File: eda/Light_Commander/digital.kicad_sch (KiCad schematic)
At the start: 40 parts, among them J14 USB_C_Receptacle_USB2.0_16P, J18 Conn_01x03, SW2 SW_Push, U1 STM32F446RETx, U10 6N137, U11 NXU0101GW, U6 USBLC6-2SC6, U8 NXU0101GW, Y1 8 MHz

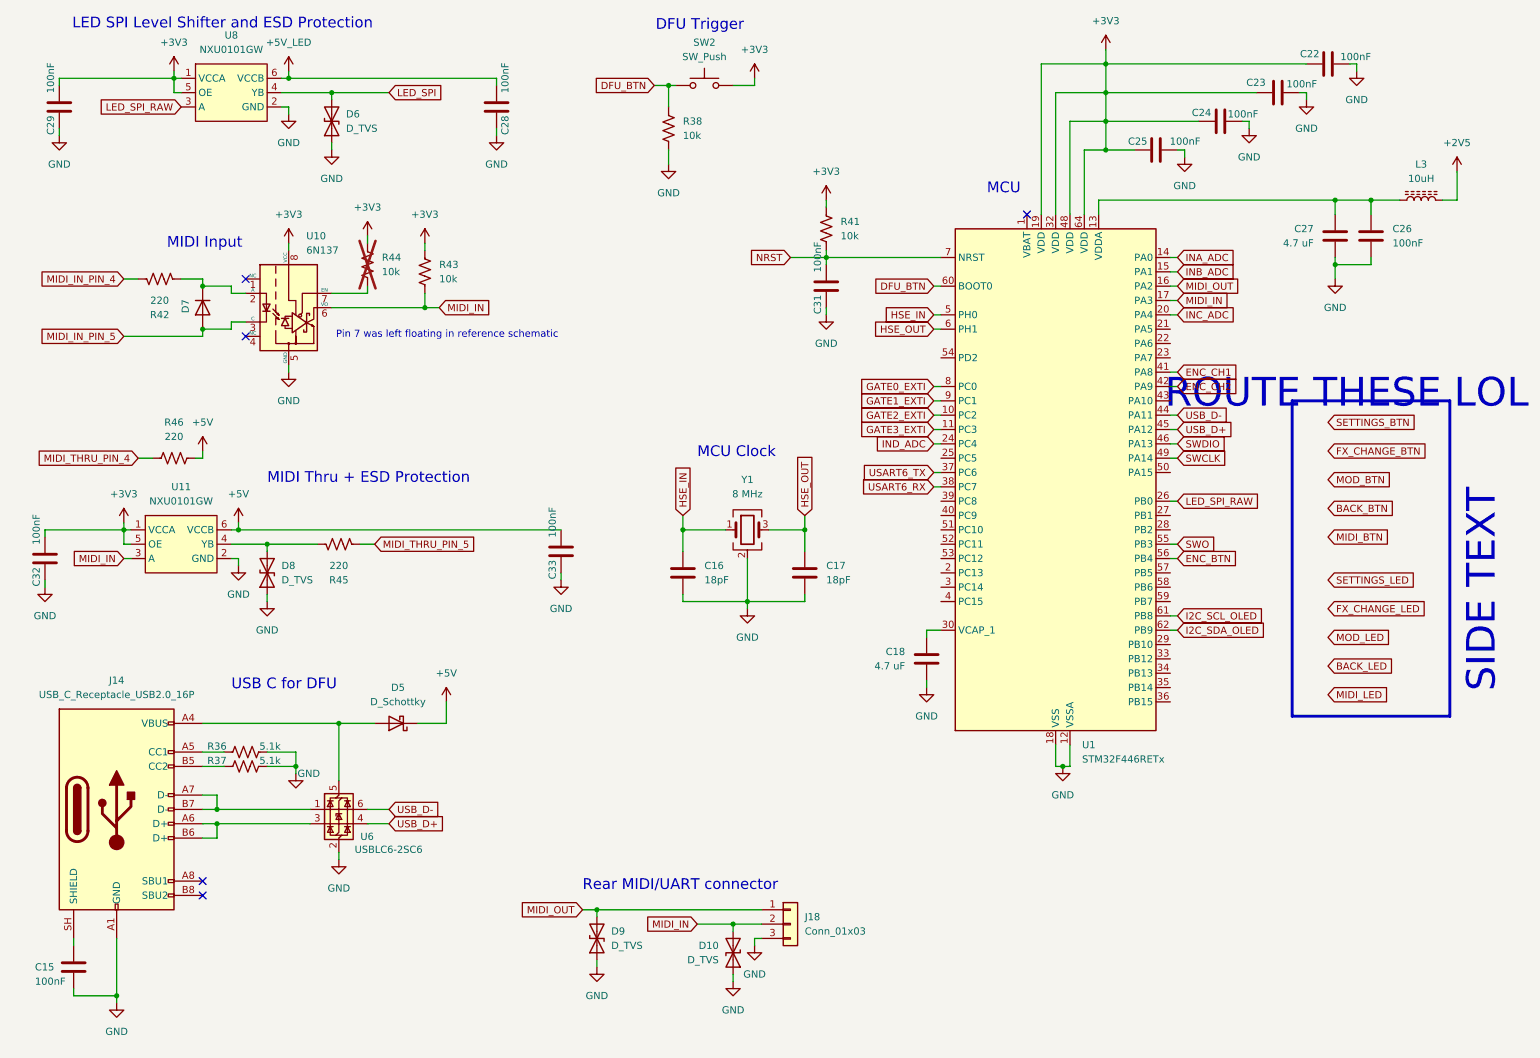
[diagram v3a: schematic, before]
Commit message: Fix footprints and finish first draft of schematic
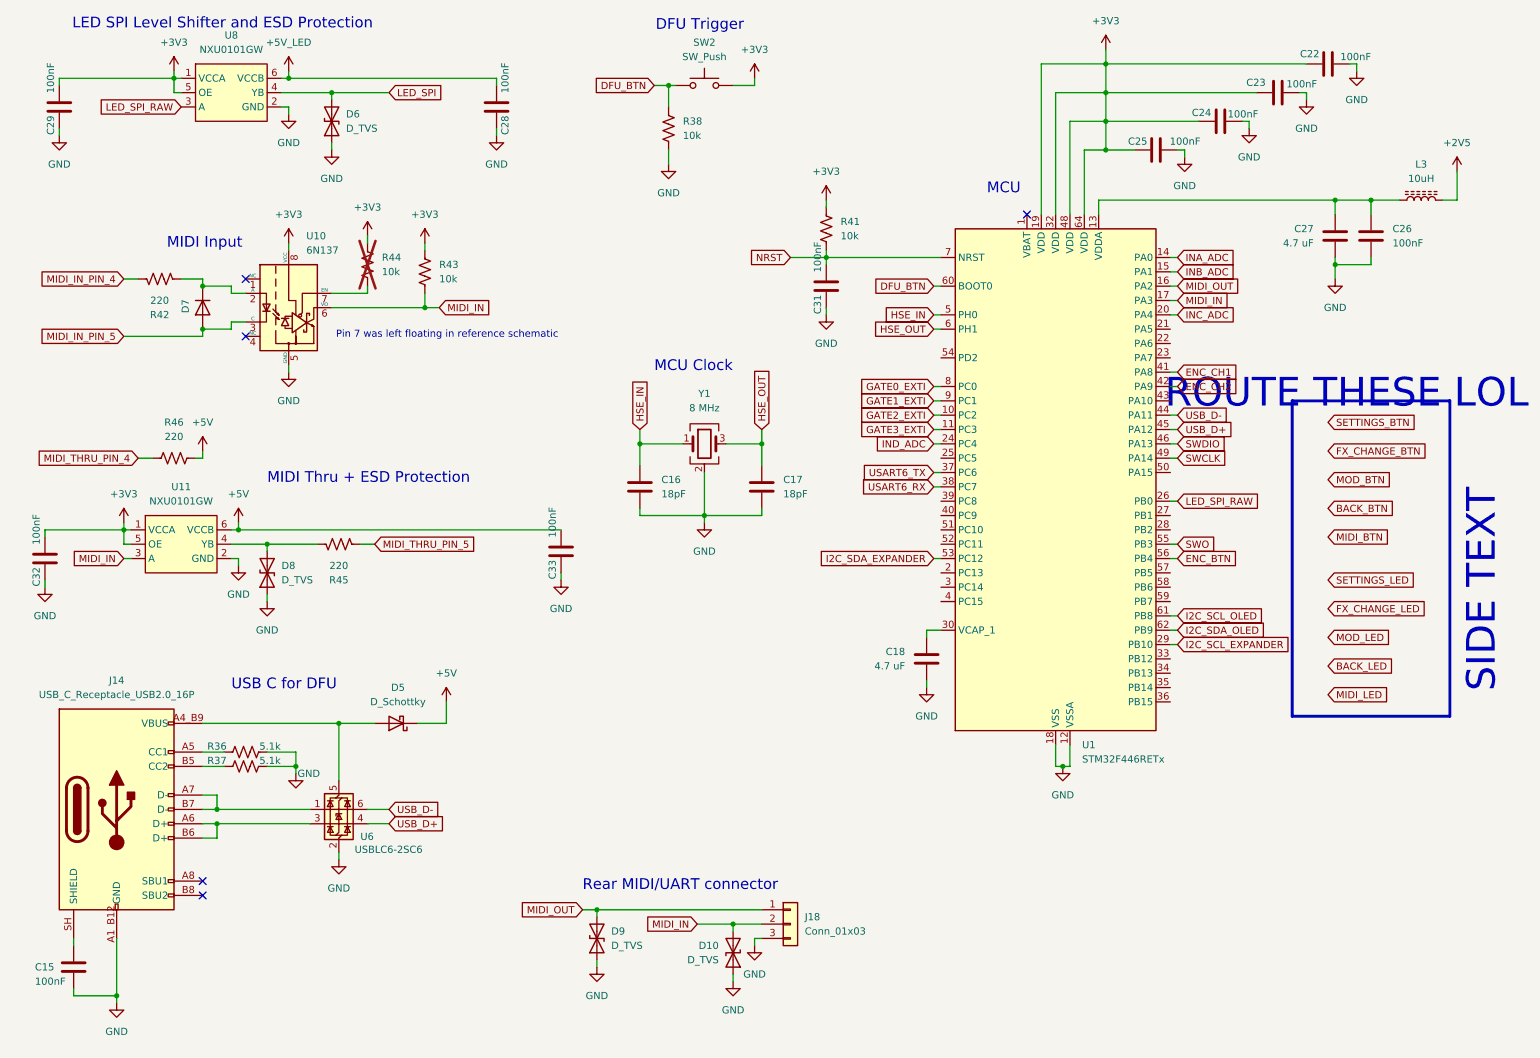
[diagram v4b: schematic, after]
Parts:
- J14: symbol Connector:USB_C_Receptacle_USB2.0_16P -> UJ20-C-H-G-SMT-1-P16-TR:USB_C_Receptacle_USB2.0_16P
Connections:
- net GND: now also J14.A1_B12 (GND), J14.B1_A12 (GND); no longer J14.A1 (GND), J14.A12 (GND), J14.B1 (GND), J14.B12 (GND)
- net I2C_SCL_EXPANDER: now reaches U1.29 (PB10)
- net I2C_SDA_EXPANDER: now reaches U1.53 (PC12)
- new net: D5.2 (A), J14.A4_B9 (VBUS), J14.B4_A9 (VBUS), U6.5 (VBUS)
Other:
- moved on the sheet: C16, C17, J14, Y1
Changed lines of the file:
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@@
 	(text "MCU Clock"
 		(exclude_from_sim no)
-		(at 133.35 90.424 0)
+		(at 125.73 75.184 0)
 		(effects
 			(font
@@
 	)
 	(junction
-		(at 152.4 104.14)
+		(at 144.78 88.9)
 		(diameter 0)
 		(color 0 0 0 0)
@@
 	)
 	(junction
-		(at 142.24 116.84)
+		(at 134.62 101.6)
 		(diameter 0)
 		(color 0 0 0 0)
@@
 	)
 	(junction
-		(at 130.81 104.14)
+		(at 123.19 88.9)
 		(diameter 0)
 		(color 0 0 0 0)
@@
 	(wire
 		(pts
-			(xy 130.81 115.57) (xy 130.81 116.84)
+			(xy 123.19 100.33) (xy 123.19 101.6)
 		)
 		(stroke
@@
 	(wire
 		(pts
-			(xy 142.24 116.84) (xy 152.4 116.84)
+			(xy 134.62 101.6) (xy 144.78 101.6)
 		)
 		(stroke
@@
 	(wire
 		(pts
-			(xy 152.4 115.57) (xy 152.4 116.84)
+			(xy 144.78 100.33) (xy 144.78 101.6)
 		)
 		(stroke
@@
 	(wire
 		(pts
-			(xy 130.81 116.84) (xy 142.24 116.84)
+			(xy 123.19 101.6) (xy 134.62 101.6)
 		)
 		(stroke
@@
 	(wire
 		(pts
-			(xy 130.81 101.6) (xy 130.81 104.14)
+			(xy 123.19 86.36) (xy 123.19 88.9)
 		)
 		(stroke
@@
 	(wire
 		(pts
-			(xy 142.24 109.22) (xy 142.24 116.84)
+			(xy 134.62 93.98) (xy 134.62 101.6)
 		)
 		(stroke
@@
 	(wire
 		(pts
-			(xy 130.81 104.14) (xy 130.81 107.95)
+			(xy 123.19 88.9) (xy 123.19 92.71)
 		)
 		(stroke
@@
 	(wire
 		(pts
+			(xy 175.26 109.22) (xy 176.53 109.22)
+		)
+		(stroke
+			(width 0)
+			(type default)
+		)
+	)
+	(wire
+		(pts
 			(xy 196.85 142.24) (xy 196.85 146.05)
 		)
@@
 	(wire
 		(pts
-			(xy 152.4 101.6) (xy 152.4 104.14)
+			(xy 144.78 86.36) (xy 144.78 88.9)
 		)
 		(stroke
@@
 	(wire
 		(pts
-			(xy 146.05 104.14) (xy 152.4 104.14)
+			(xy 138.43 88.9) (xy 144.78 88.9)
 		)
 		(stroke
@@
 	(wire
 		(pts
-			(xy 152.4 104.14) (xy 152.4 107.95)
+			(xy 144.78 88.9) (xy 144.78 92.71)
 		)
 		(stroke
@@
 	(wire
 		(pts
-			(xy 142.24 116.84) (xy 142.24 118.11)
+			(xy 134.62 101.6) (xy 134.62 102.87)
 		)
 		(stroke
@@
 	(wire
 		(pts
+			(xy 218.44 124.46) (xy 217.17 124.46)
+		)
+		(stroke
+			(width 0)
+			(type default)
+		)
+	)
+	(wire
+		(pts
 			(xy 17.78 104.14) (xy 31.75 104.14)
 		)
@@
 	(wire
 		(pts
-			(xy 130.81 104.14) (xy 138.43 104.14)
+			(xy 123.19 88.9) (xy 130.81 88.9)
 		)
 		(stroke
@@
 	(global_label "HSE_OUT"
 		(shape input)
-		(at 152.4 101.6 90)
+		(at 144.78 86.36 90)
 		(fields_autoplaced yes)
 		(effects
@@
 		)
 		(property "Intersheetrefs" "${INTERSHEET_REFS}"
-			(at 152.4 90.3296 90)
+			(at 144.78 75.0896 90)
 			(hide yes)
 			(show_name no)
@@
 	(global_label "HSE_IN"
 		(shape input)
-		(at 130.81 101.6 90)
+		(at 123.19 86.36 90)
 		(fields_autoplaced yes)
 		(effects
@@
 		)
 		(property "Intersheetrefs" "${INTERSHEET_REFS}"
-			(at 130.81 92.0229 90)
+			(at 123.19 76.7829 90)
 			(hide yes)
 			(show_name no)
@@
 		)
 	)
+	(global_label "I2C_SCL_EXPANDER"
+		(shape input)
+		(at 218.44 124.46 0)
+		(fields_autoplaced yes)
+		(effects
+			(font
+				(size 1.27 1.27)
+			)
+			(justify left)
+		)
+		(property "Intersheetrefs" "${INTERSHEET_REFS}"
+			(at 239.6889 124.46 0)
+			(hide yes)
+			(show_name no)
+			(do_not_autoplace no)
+			(effects
+				(font
+					(size 1.27 1.27)
+				)
+				(justify left)
+			)
+		)
+	)
 	(global_label "MIDI_IN"
 		(shape input)
@@
 		)
 	)
+	(global_label "I2C_SDA_EXPANDER"
+		(shape input)
+		(at 175.26 109.22 180)
+		(fields_autoplaced yes)
+		(effects
+			(font
+				(size 1.27 1.27)
+			)
+			(justify right)
+		)
+		(property "Intersheetrefs" "${INTERSHEET_REFS}"
+			(at 153.9506 109.22 0)
+			(hide yes)
+			(show_name no)
+			(do_not_autoplace no)
+			(effects
+				(font
+					(size 1.27 1.27)
+				)
+				(justify right)
+			)
+		)
+	)
 	(global_label "MIDI_BTN"
 		(shape input)
@@
 	)
 	(symbol
-		(lib_id "Connector:USB_C_Receptacle_USB2.0_16P")
+		(lib_id "UJ20-C-H-G-SMT-1-P16-TR:USB_C_Receptacle_USB2.0_16P")
 		(at 30.48 153.67 0)
 		(unit 1)
@@
 			)
 		)
-		(pin "A1"
+		(pin "B1_A12"
 		)
-		(pin "A9"
+		(pin "A1_B12"
 		)
 		(pin "A7"
@@
 		(pin "B8"
 		)
-		(pin "A4"
-		)
 		(pin "A6"
 		)
-		(pin "B1"
+		(pin "A4_B9"
 		)
-		(pin "B4"
+		(pin "B4_A9"
 		)
 		(pin "B5"
@@
 		(pin "B6"
 		)
-		(pin "A12"
-		)
 		(pin "B7"
 		)
-		(pin "B9"
-		)
-		(pin "B12"
-		)
 		(pin "SH"
 		)
@@
 	(symbol
 		(lib_id "Device:C")
-		(at 130.81 111.76 0)
+		(at 123.19 96.52 0)
 		(unit 1)
 		(body_style 1)
@@
 		(fields_autoplaced yes)
 		(property "Reference" "C16"
-			(at 134.62 110.4899 0)
+			(at 127 95.2499 0)
 			(show_name no)
 			(do_not_autoplace no)
@@
 		)
 		(property "Value" "18pF"
-			(at 134.62 113.0299 0)
+			(at 127 97.7899 0)
 			(show_name no)
 			(do_not_autoplace no)
@@
 		)
 		(property "Footprint" "Capacitor_SMD:C_0402_1005Metric"
-			(at 131.7752 115.57 0)
+			(at 124.1552 100.33 0)
 			(hide yes)
 			(show_name no)
@@
 		)
 		(property "Datasheet" ""
-			(at 130.81 111.76 0)
+			(at 123.19 96.52 0)
 			(hide yes)
 			(show_name no)
@@
 		)
 		(property "Description" "Unpolarized capacitor"
-			(at 130.81 111.76 0)
+			(at 123.19 96.52 0)
 			(hide yes)
 			(show_name no)
@@
 		)
 		(property "Digikey_PN" "490-5858-1-ND"
-			(at 130.81 111.76 0)
+			(at 123.19 96.52 0)
 			(hide yes)
 			(show_name no)
@@
 	(symbol
 		(lib_id "power:GND")
-		(at 142.24 118.11 0)
+		(at 134.62 102.87 0)
 		(unit 1)
 		(body_style 1)
@@
 		(fields_autoplaced yes)
 		(property "Reference" "#PWR073"
-			(at 142.24 124.46 0)
+			(at 134.62 109.22 0)
 			(hide yes)
 			(show_name no)
@@
 		)
 		(property "Value" "GND"
-			(at 142.24 123.19 0)
+			(at 134.62 107.95 0)
 			(show_name no)
 			(do_not_autoplace no)
@@
 		)
 		(property "Footprint" ""
-			(at 142.24 118.11 0)
+			(at 134.62 102.87 0)
 			(hide yes)
 			(show_name no)
@@
 		)
 		(property "Datasheet" ""
-			(at 142.24 118.11 0)
+			(at 134.62 102.87 0)
 			(hide yes)
 			(show_name no)
@@
 		)
 		(property "Description" "Power symbol creates a global label with name \"GND\" , ground"
-			(at 142.24 118.11 0)
+			(at 134.62 102.87 0)
 			(hide yes)
 			(show_name no)
@@
 	(symbol
 		(lib_id "Device:Crystal_GND24")
-		(at 142.24 104.14 0)
+		(at 134.62 88.9 0)
 		(unit 1)
 		(body_style 1)
@@
 		(fields_autoplaced yes)
 		(property "Reference" "Y1"
-			(at 142.24 95.25 0)
+			(at 134.62 80.01 0)
 			(show_name no)
 			(do_not_autoplace no)
@@
 		)
 		(property "Value" "8 MHz"
-			(at 142.24 97.79 0)
+			(at 134.62 82.55 0)
 			(show_name no)
 			(do_not_autoplace no)
@@
 		)
 		(property "Footprint" "footprints:ECS-80-18-33-JGN-TR"
-			(at 142.24 104.14 0)
+			(at 134.62 88.9 0)
 			(hide yes)
 			(show_name no)
@@
 		)
 		(property "Datasheet" ""
-			(at 142.24 104.14 0)
+			(at 134.62 88.9 0)
 			(hide yes)
 			(show_name no)
@@
 		)
 		(property "Description" "Four pin crystal, GND on pins 2 and 4"
-			(at 142.24 104.14 0)
+			(at 134.62 88.9 0)
 			(hide yes)
 			(show_name no)
@@
 		)
 		(property private "KLC_S3.3" "The rectangle is not a symbol body but a graphical element"
-			(at 142.24 116.84 0)
+			(at 134.62 101.6 0)
 			(hide yes)
 			(show_name yes)
@@
 		)
 		(property private "KLC_S4.1" "Some pins are on 50mil grid to make the symbol small"
-			(at 142.24 119.38 0)
+			(at 134.62 104.14 0)
 			(hide yes)
 			(show_name yes)
@@
 		)
 		(property "Digikey_PN" "50-ECS-80-18-33-JGN-CT-ND"
-			(at 142.24 104.14 0)
+			(at 134.62 88.9 0)
 			(hide yes)
 			(show_name no)
@@
 	(symbol
 		(lib_id "Device:C")
-		(at 152.4 111.76 0)
+		(at 144.78 96.52 0)
 		(unit 1)
 		(body_style 1)
@@
 		(fields_autoplaced yes)
 		(property "Reference" "C17"
-			(at 156.21 110.4899 0)
+			(at 148.59 95.2499 0)
 			(show_name no)
 			(do_not_autoplace no)
@@
 		)
 		(property "Value" "18pF"
-			(at 156.21 113.0299 0)
+			(at 148.59 97.7899 0)
 			(show_name no)
 			(do_not_autoplace no)
@@
 		)
 		(property "Footprint" "Capacitor_SMD:C_0402_1005Metric"
-			(at 153.3652 115.57 0)
+			(at 145.7452 100.33 0)
 			(hide yes)
 			(show_name no)
@@
 		)
 		(property "Datasheet" ""
-			(at 152.4 111.76 0)
+			(at 144.78 96.52 0)
 			(hide yes)
 			(show_name no)
@@
 		)
 		(property "Description" "Unpolarized capacitor"
-			(at 152.4 111.76 0)
+			(at 144.78 96.52 0)
 			(hide yes)
 			(show_name no)
@@
 		)
 		(property "Digikey_PN" "490-5858-1-ND"
-			(at 152.4 111.76 0)
+			(at 144.78 96.52 0)
 			(hide yes)
 			(show_name no)

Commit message: Initial component placement
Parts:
- U11: Digikey_PN (none) -> 1727-NXU0101GWHCT-ND
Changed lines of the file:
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@@
+			)
+		)
+		(property "Digikey_PN" "1727-NXU0101GWHCT-ND"
+			(at 41.91 106.68 0)
+			(hide yes)
+			(show_name no)
+			(do_not_autoplace no)
+			(effects
+				(font
+					(size 1.27 1.27)
+				)
 			)
 		)

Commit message: Add remaining IO from schematic to CubeMX project
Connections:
- net BACK_BTN: now also U1.23 (PA7)
- net BACK_LED: now also U1.35 (PB14)
- net FX_CHANGE_BTN: now also U1.43 (PA10)
- net FX_CHANGE_LED: now also U1.33 (PB12)
- net MIDI_BTN: now also U1.2 (PC13)
- net MIDI_LED: now also U1.27 (PB1)
- net MOD_BTN: now also U1.57 (PB5)
- net MOD_LED: now also U1.34 (PB13)
- net SETTINGS_BTN: now also U1.58 (PB6)
- net SETTINGS_LED: now also U1.28 (PB2)
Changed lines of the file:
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@@
+	(wire
+		(pts
+			(xy 218.44 132.08) (xy 217.17 132.08)
+		)
+		(stroke
+			(width 0)
+			(type default)
+		)
+	)
 	(wire
 		(pts
@@
 	(wire
 		(pts
+			(xy 218.44 104.14) (xy 217.17 104.14)
+		)
+		(stroke
+			(width 0)
+			(type default)
+		)
+	)
+	(wire
+		(pts
 			(xy 45.72 156.21) (xy 48.26 156.21)
 		)
@@
 	(wire
 		(pts
+			(xy 175.26 111.76) (xy 176.53 111.76)
+		)
+		(stroke
+			(width 0)
+			(type default)
+		)
+	)
+	(wire
+		(pts
 			(xy 50.8 67.31) (xy 50.8 68.58)
 		)
@@
 	(wire
 		(pts
+			(xy 218.44 129.54) (xy 217.17 129.54)
+		)
+		(stroke
+			(width 0)
+			(type default)
+		)
+	)
+	(wire
+		(pts
+			(xy 218.44 73.66) (xy 217.17 73.66)
+		)
+		(stroke
+			(width 0)
+			(type default)
+		)
+	)
+	(wire
+		(pts
 			(xy 17.78 113.03) (xy 17.78 114.3)
 		)
@@
 	(wire
 		(pts
+			(xy 218.44 101.6) (xy 217.17 101.6)
+		)
+		(stroke
+			(width 0)
+			(type default)
+		)
+	)
+	(wire
+		(pts
 			(xy 218.44 88.9) (xy 217.17 88.9)
 		)
@@
 	(wire
 		(pts
+			(xy 218.44 114.3) (xy 217.17 114.3)
+		)
+		(stroke
+			(width 0)
+			(type default)
+		)
+	)
+	(wire
+		(pts
 			(xy 50.8 60.96) (xy 50.8 62.23)
 		)
@@
 	(wire
 		(pts
+			(xy 218.44 111.76) (xy 217.17 111.76)
+		)
+		(stroke
+			(width 0)
+			(type default)
+		)
+	)
+	(wire
+		(pts
 			(xy 45.72 91.44) (xy 44.45 91.44)
 		)
@@
 	(wire
 		(pts
+			(xy 218.44 127) (xy 217.17 127)
+		)
+		(stroke
+			(width 0)
+			(type default)
+		)
+	)
+	(wire
+		(pts
 			(xy 78.74 26.67) (xy 68.58 26.67)
 		)
@@
 	(wire
 		(pts
+			(xy 218.44 81.28) (xy 217.17 81.28)
+		)
+		(stroke
+			(width 0)
+			(type default)
+		)
+	)
+	(wire
+		(pts
 			(xy 31.75 69.85) (xy 45.72 69.85)
 		)
@@
 	(global_label "BACK_LED"
 		(shape input)
-		(at 245.11 128.27 0)
-		(fields_autoplaced yes)
-		(effects
-			(font
-				(size 1.27 1.27)
-			)
-			(justify left)
-		)
-		(property "Intersheetrefs" "${INTERSHEET_REFS}"
-			(at 257.4085 128.27 0)
+		(at 218.44 132.08 0)
+		(fields_autoplaced yes)
+		(effects
+			(font
+				(size 1.27 1.27)
+			)
+			(justify left)
+		)
+		(property "Intersheetrefs" "${INTERSHEET_REFS}"
+			(at 230.7385 132.08 0)
 			(hide yes)
 			(show_name no)
@@
 	(global_label "MOD_BTN"
 		(shape input)
-		(at 245.11 95.25 0)
-		(fields_autoplaced yes)
-		(effects
-			(font
-				(size 1.27 1.27)
-			)
-			(justify left)
-		)
-		(property "Intersheetrefs" "${INTERSHEET_REFS}"
-			(at 256.6828 95.25 0)
+		(at 218.44 111.76 0)
+		(fields_autoplaced yes)
+		(effects
+			(font
+				(size 1.27 1.27)
+			)
+			(justify left)
+		)
+		(property "Intersheetrefs" "${INTERSHEET_REFS}"
+			(at 230.0128 111.76 0)
 			(hide yes)
 			(show_name no)
@@
 	(global_label "SETTINGS_LED"
 		(shape input)
-		(at 245.11 113.03 0)
+		(at 218.44 104.14 0)
 		(fields_autoplaced yes)
 		(effects
@@
 		)
 		(property "Intersheetrefs" "${INTERSHEET_REFS}"
-			(at 261.2184 113.03 0)
+			(at 234.5484 104.14 0)
 			(hide yes)
 			(show_name no)
@@
 	(global_label "FX_CHANGE_LED"
 		(shape input)
-		(at 245.11 118.11 0)
+		(at 218.44 127 0)
 		(fields_autoplaced yes)
 		(effects
@@
 		)
 		(property "Intersheetrefs" "${INTERSHEET_REFS}"
-			(at 263.2142 118.11 0)
+			(at 236.5442 127 0)
 			(hide yes)
 			(show_name no)
@@
 	(global_label "MOD_LED"
 		(shape input)
-		(at 245.11 123.19 0)
-		(fields_autoplaced yes)
-		(effects
-			(font
-				(size 1.27 1.27)
-			)
-			(justify left)
-		)
-		(property "Intersheetrefs" "${INTERSHEET_REFS}"
-			(at 256.5618 123.19 0)
+		(at 218.44 129.54 0)
+		(fields_autoplaced yes)
+		(effects
+			(font
+				(size 1.27 1.27)
+			)
+			(justify left)
+		)
+		(property "Intersheetrefs" "${INTERSHEET_REFS}"
+			(at 229.8918 129.54 0)
 			(hide yes)
 			(show_name no)
@@
 	(global_label "MIDI_BTN"
 		(shape input)
-		(at 245.11 105.41 0)
-		(fields_autoplaced yes)
-		(effects
-			(font
-				(size 1.27 1.27)
-			)
-			(justify left)
-		)
-		(property "Intersheetrefs" "${INTERSHEET_REFS}"
-			(at 256.5619 105.41 0)
-			(hide yes)
-			(show_name no)
-			(do_not_autoplace no)
-			(effects
-				(font
-					(size 1.27 1.27)
-				)
-				(justify left)
+		(at 175.26 111.76 180)
+		(fields_autoplaced yes)
+		(effects
+			(font
+				(size 1.27 1.27)
+			)
+			(justify right)
+		)
+		(property "Intersheetrefs" "${INTERSHEET_REFS}"
+			(at 163.8081 111.76 0)
+			(hide yes)
+			(show_name no)
+			(do_not_autoplace no)
+			(effects
+				(font
+					(size 1.27 1.27)
+				)
+				(justify right)
 			)
 		)
@@
 	(global_label "BACK_BTN"
 		(shape input)
-		(at 245.11 100.33 0)
-		(fields_autoplaced yes)
-		(effects
-			(font
-				(size 1.27 1.27)
-			)
-			(justify left)
-		)
-		(property "Intersheetrefs" "${INTERSHEET_REFS}"
-			(at 257.5295 100.33 0)
+		(at 218.44 73.66 0)
+		(fields_autoplaced yes)
+		(effects
+			(font
+				(size 1.27 1.27)
+			)
+			(justify left)
+		)
+		(property "Intersheetrefs" "${INTERSHEET_REFS}"
+			(at 230.8595 73.66 0)
 			(hide yes)
 			(show_name no)
@@
 	(global_label "SETTINGS_BTN"
 		(shape input)
-		(at 245.11 85.09 0)
+		(at 218.44 114.3 0)
 		(fields_autoplaced yes)
 		(effects
@@
 		)
 		(property "Intersheetrefs" "${INTERSHEET_REFS}"
-			(at 261.3394 85.09 0)
+			(at 234.6694 114.3 0)
 			(hide yes)
 			(show_name no)
@@
 	(global_label "MIDI_LED"
 		(shape input)
-		(at 245.11 133.35 0)
-		(fields_autoplaced yes)
-		(effects
-			(font
-				(size 1.27 1.27)
-			)
-			(justify left)
-		)
-		(property "Intersheetrefs" "${INTERSHEET_REFS}"
-			(at 256.4409 133.35 0)
+		(at 218.44 101.6 0)
+		(fields_autoplaced yes)
+		(effects
+			(font
+				(size 1.27 1.27)
+			)
+			(justify left)
+		)
+		(property "Intersheetrefs" "${INTERSHEET_REFS}"
+			(at 229.7709 101.6 0)
 			(hide yes)
 			(show_name no)
@@
 	(global_label "FX_CHANGE_BTN"
 		(shape input)
-		(at 245.11 90.17 0)
+		(at 218.44 81.28 0)
 		(fields_autoplaced yes)
 		(effects
@@
 		)
 		(property "Intersheetrefs" "${INTERSHEET_REFS}"
-			(at 263.3352 90.17 0)
-			(hide yes)
-			(show_name no)
+			(at 236.6652 81.28 0)
+			(hide yes)
+			(show_name no)
